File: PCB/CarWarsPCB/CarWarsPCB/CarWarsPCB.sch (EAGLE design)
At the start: 14 parts, among them J1 MAGJACK

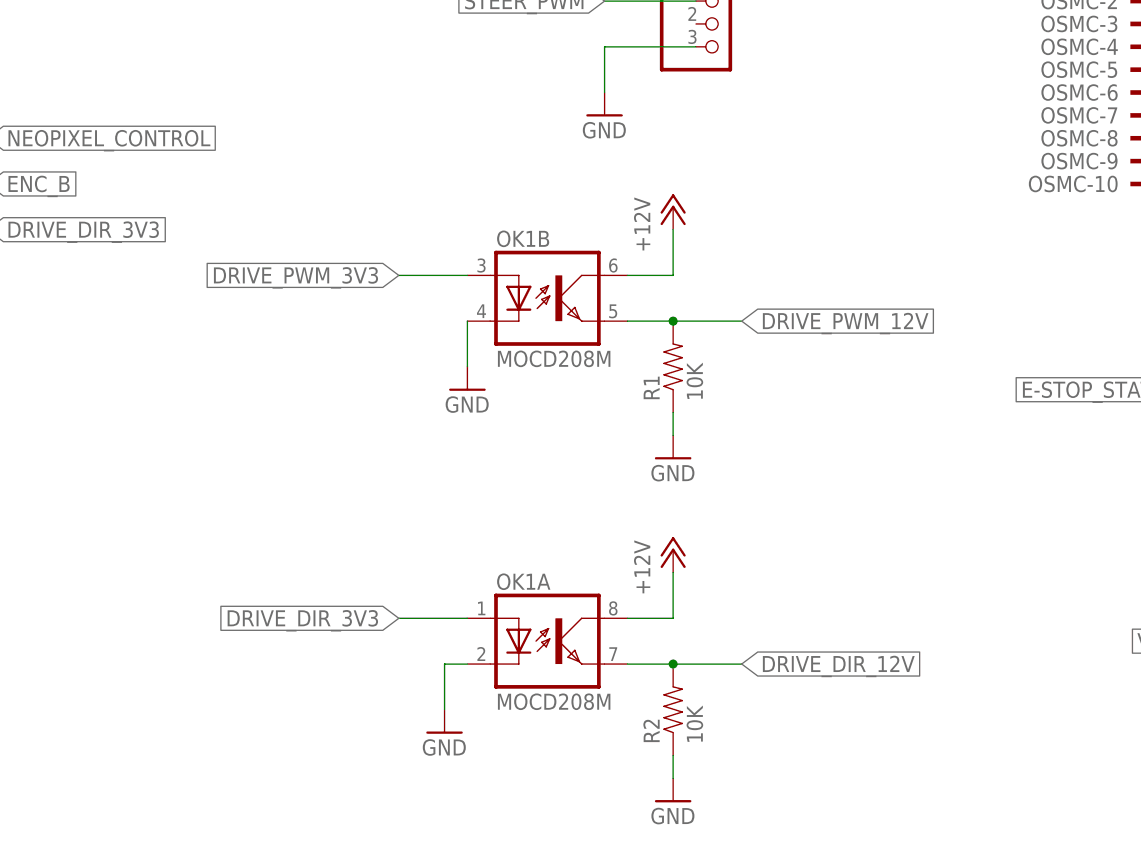
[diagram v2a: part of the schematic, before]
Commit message: CarWars PCB Prototype finalization
Implements Ryo's recommended changes to OSMC
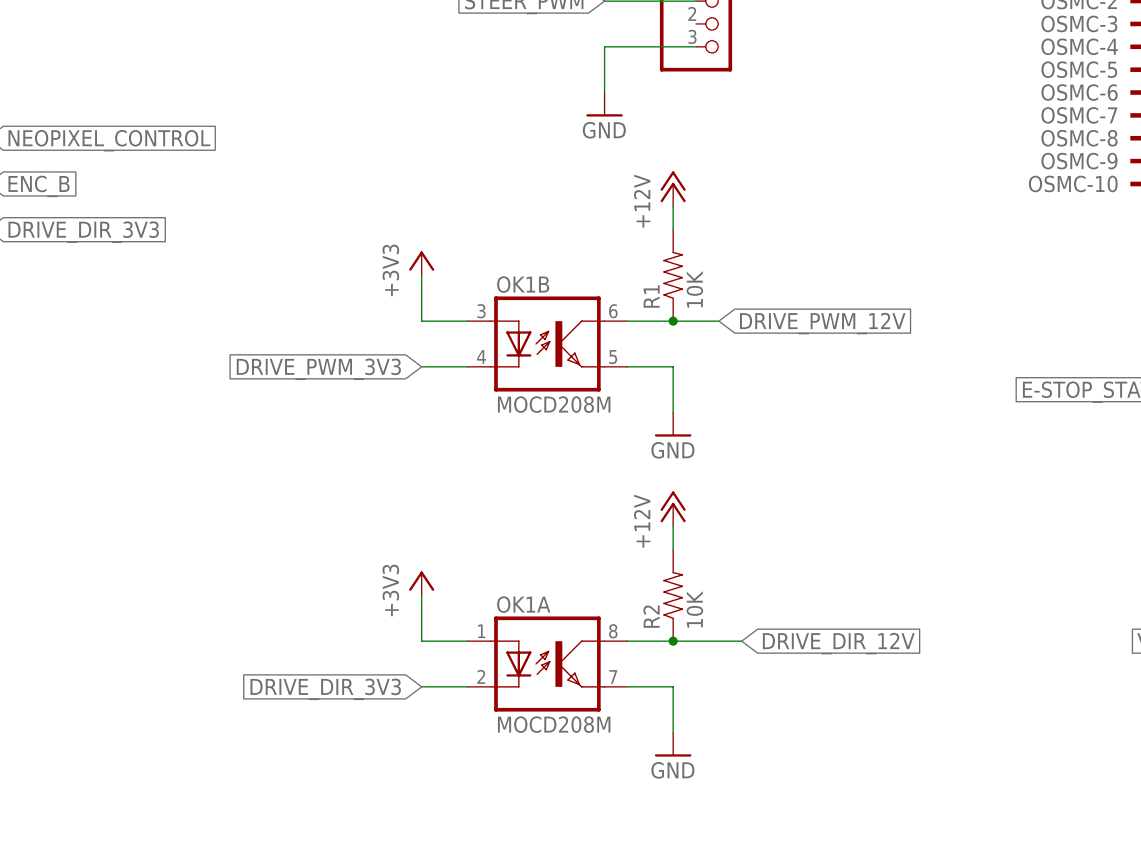
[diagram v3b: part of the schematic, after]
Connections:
- net +12V: now also R1.2, R2.2; no longer OK1A.COL, OK1B.COL
- net +3V3: now also OK1A.A, OK1B.A
- net DRIVE_DIR_12V: now also OK1A.COL, R2.1; no longer OK1A.EMIT, R2.2
- net DRIVE_DIR_3V3: now also OK1A.C; no longer OK1A.A
- net DRIVE_PWM_12V: now also OK1B.COL, R1.1; no longer OK1B.EMIT, R1.2
- net DRIVE_PWM_3V3: now also OK1B.C; no longer OK1B.A
- net GND: now also OK1A.EMIT, OK1B.EMIT; no longer OK1A.C, OK1B.C, R1.1, R2.1
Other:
- moved on the sheet: OK1A, OK1B, R1, R2
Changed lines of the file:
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@@
 <part name="GND6" library="supply1" library_urn="urn:adsk.eagle:library:371" deviceset="GND" device=""/>
 <part name="OSMC" library="con-3m" library_urn="urn:adsk.eagle:library:119" deviceset="2510-" device=""/>
-<part name="GND4" library="supply1" library_urn="urn:adsk.eagle:library:371" deviceset="GND" device=""/>
 <part name="GND7" library="supply1" library_urn="urn:adsk.eagle:library:371" deviceset="GND" device=""/>
 <part name="R1" library="SparkFun-Resistors" deviceset="10KOHM-1/10W-1%(0603)" device="0603" value="10K"/>
@@
 <part name="R2" library="SparkFun-Resistors" deviceset="10KOHM-1/10W-1%(0603)" device="0603" value="10K"/>
 <part name="GND8" library="supply1" library_urn="urn:adsk.eagle:library:371" deviceset="GND" device=""/>
-<part name="GND9" library="supply1" library_urn="urn:adsk.eagle:library:371" deviceset="GND" device=""/>
 <part name="GND10" library="supply1" library_urn="urn:adsk.eagle:library:371" deviceset="GND" device=""/>
 <part name="P+7" library="supply1" library_urn="urn:adsk.eagle:library:371" deviceset="+12V" device=""/>
@@
 <part name="P+9" library="supply1" library_urn="urn:adsk.eagle:library:371" deviceset="VCC" device=""/>
 <part name="IV_SENSOR" library="Roboracing" deviceset="PINHD-1X3" device=""/>
+<part name="+3V3" library="supply1" library_urn="urn:adsk.eagle:library:371" deviceset="+3V3" device=""/>
+<part name="+3V4" library="supply1" library_urn="urn:adsk.eagle:library:371" deviceset="+3V3" device=""/>
 </parts>
 <sheets>
@@
 <instance part="OSMC" gate="-9" x="266.7" y="43.18"/>
 <instance part="OSMC" gate="-10" x="266.7" y="40.64"/>
-<instance part="GND4" gate="1" x="193.04" y="17.78"/>
-<instance part="GND7" gate="1" x="215.9" y="10.16"/>
-<instance part="R1" gate="G$1" x="215.9" y="20.32" rot="R90"/>
-<instance part="OK1" gate="A" x="203.2" y="-10.16"/>
-<instance part="R2" gate="G$1" x="215.9" y="-17.78" rot="R90"/>
-<instance part="GND8" gate="1" x="215.9" y="-27.94"/>
-<instance part="GND9" gate="1" x="190.5" y="-20.32"/>
+<instance part="GND7" gate="1" x="215.9" y="12.7"/>
+<instance part="R1" gate="G$1" x="215.9" y="30.48" rot="R90"/>
+<instance part="OK1" gate="A" x="203.2" y="-12.7"/>
+<instance part="R2" gate="G$1" x="215.9" y="-5.08" rot="R90"/>
+<instance part="GND8" gate="1" x="215.9" y="-22.86"/>
 <instance part="GND10" gate="1" x="279.4" y="35.56"/>
 <instance part="P+7" gate="1" x="284.48" y="73.66"/>
-<instance part="P+4" gate="1" x="215.9" y="38.1"/>
-<instance part="P+5" gate="1" x="215.9" y="0"/>
-<instance part="OK1" gate="B" x="203.2" y="27.94"/>
+<instance part="P+4" gate="1" x="215.9" y="40.64"/>
+<instance part="P+5" gate="1" x="215.9" y="5.08"/>
+<instance part="OK1" gate="B" x="203.2" y="22.86"/>
 <instance part="LIGHTS" gate="A" x="314.96" y="106.68"/>
 <instance part="GND11" gate="1" x="304.8" y="99.06"/>
@@
 <instance part="P+9" gate="VCC" x="30.48" y="88.9"/>
 <instance part="IV_SENSOR" gate="A" x="299.72" y="-10.16"/>
+<instance part="+3V3" gate="G$1" x="187.96" y="33.02"/>
+<instance part="+3V4" gate="G$1" x="187.96" y="-2.54"/>
 </instances>
 <busses>
@@
 </segment>
 <segment>
-<wire x1="193.04" y1="25.4" x2="193.04" y2="20.32" width="0.1524" layer="91"/>
-<pinref part="GND4" gate="1" pin="GND"/>
-<pinref part="OK1" gate="B" pin="C"/>
-</segment>
-<segment>
-<pinref part="GND7" gate="1" pin="GND"/>
-<pinref part="R1" gate="G$1" pin="1"/>
-<wire x1="215.9" y1="12.7" x2="215.9" y2="15.24" width="0.1524" layer="91"/>
-</segment>
-<segment>
-<pinref part="OK1" gate="A" pin="C"/>
-<pinref part="GND9" gate="1" pin="GND"/>
-<wire x1="193.04" y1="-12.7" x2="190.5" y2="-12.7" width="0.1524" layer="91"/>
-<wire x1="190.5" y1="-12.7" x2="190.5" y2="-17.78" width="0.1524" layer="91"/>
-</segment>
-<segment>
-<pinref part="GND8" gate="1" pin="GND"/>
-<pinref part="R2" gate="G$1" pin="1"/>
-<wire x1="215.9" y1="-25.4" x2="215.9" y2="-22.86" width="0.1524" layer="91"/>
-</segment>
-<segment>
 <pinref part="OSMC" gate="-10" pin="KL"/>
 <pinref part="GND10" gate="1" pin="GND"/>
@@
 <label x="292.1" y="-12.7" size="1.778" layer="95" rot="R180" xref="yes"/>
 </segment>
+<segment>
+<pinref part="OK1" gate="B" pin="EMIT"/>
+<pinref part="GND7" gate="1" pin="GND"/>
+<wire x1="210.82" y1="20.32" x2="215.9" y2="20.32" width="0.1524" layer="91"/>
+<wire x1="215.9" y1="20.32" x2="215.9" y2="15.24" width="0.1524" layer="91"/>
+</segment>
+<segment>
+<pinref part="OK1" gate="A" pin="EMIT"/>
+<pinref part="GND8" gate="1" pin="GND"/>
+<wire x1="210.82" y1="-15.24" x2="215.9" y2="-15.24" width="0.1524" layer="91"/>
+<wire x1="215.9" y1="-15.24" x2="215.9" y2="-20.32" width="0.1524" layer="91"/>
+</segment>
 </net>
 <net name="+3V3" class="0">
@@
 <wire x1="119.38" y1="81.28" x2="119.38" y2="86.36" width="0.1524" layer="91"/>
 </segment>
+<segment>
+<pinref part="OK1" gate="B" pin="A"/>
+<pinref part="+3V3" gate="G$1" pin="+3V3"/>
+<wire x1="193.04" y1="25.4" x2="187.96" y2="25.4" width="0.1524" layer="91"/>
+<wire x1="187.96" y1="25.4" x2="187.96" y2="30.48" width="0.1524" layer="91"/>
+</segment>
+<segment>
+<pinref part="OK1" gate="A" pin="A"/>
+<pinref part="+3V4" gate="G$1" pin="+3V3"/>
+<wire x1="193.04" y1="-10.16" x2="187.96" y2="-10.16" width="0.1524" layer="91"/>
+<wire x1="187.96" y1="-10.16" x2="187.96" y2="-5.08" width="0.1524" layer="91"/>
+</segment>
 </net>
 <net name="DRIVE_PWM_3V3" class="0">
@@
 </segment>
 <segment>
-<wire x1="193.04" y1="30.48" x2="185.42" y2="30.48" width="0.1524" layer="91"/>
-<label x="185.42" y="30.48" size="1.778" layer="95" rot="R180" xref="yes"/>
-<pinref part="OK1" gate="B" pin="A"/>
+<pinref part="OK1" gate="B" pin="C"/>
+<wire x1="193.04" y1="20.32" x2="187.96" y2="20.32" width="0.1524" layer="91"/>
+<label x="187.96" y="20.32" size="1.778" layer="95" rot="R180" xref="yes"/>
 </segment>
 </net>
@@
 <net name="DRIVE_PWM_12V" class="0">
 <segment>
-<wire x1="210.82" y1="25.4" x2="215.9" y2="25.4" width="0.1524" layer="91"/>
-<pinref part="R1" gate="G$1" pin="2"/>
-<wire x1="215.9" y1="25.4" x2="223.52" y2="25.4" width="0.1524" layer="91"/>
-<junction x="215.9" y="25.4"/>
-<label x="223.52" y="25.4" size="1.778" layer="95" xref="yes"/>
-<pinref part="OK1" gate="B" pin="EMIT"/>
-</segment>
-<segment>
 <pinref part="OSMC" gate="-6" pin="KL"/>
 <wire x1="271.78" y1="50.8" x2="289.56" y2="50.8" width="0.1524" layer="91"/>
 <label x="289.56" y="50.8" size="1.778" layer="95" xref="yes"/>
 </segment>
+<segment>
+<pinref part="OK1" gate="B" pin="COL"/>
+<pinref part="R1" gate="G$1" pin="1"/>
+<wire x1="210.82" y1="25.4" x2="215.9" y2="25.4" width="0.1524" layer="91"/>
+<wire x1="215.9" y1="25.4" x2="220.98" y2="25.4" width="0.1524" layer="91"/>
+<junction x="215.9" y="25.4"/>
+<label x="220.98" y="25.4" size="1.778" layer="95" xref="yes"/>
+</segment>
 </net>
 <net name="DRIVE_DIR_12V" class="0">
-<segment>
-<pinref part="OK1" gate="A" pin="EMIT"/>
-<wire x1="210.82" y1="-12.7" x2="215.9" y2="-12.7" width="0.1524" layer="91"/>
-<pinref part="R2" gate="G$1" pin="2"/>
-<wire x1="215.9" y1="-12.7" x2="223.52" y2="-12.7" width="0.1524" layer="91"/>
-<junction x="215.9" y="-12.7"/>
-<label x="223.52" y="-12.7" size="1.778" layer="95" xref="yes"/>
-</segment>
 <segment>
 <pinref part="OSMC" gate="-8" pin="KL"/>
@@
 <label x="289.56" y="45.72" size="1.778" layer="95" xref="yes"/>
 </segment>
+<segment>
+<pinref part="OK1" gate="A" pin="COL"/>
+<pinref part="R2" gate="G$1" pin="1"/>
+<wire x1="210.82" y1="-10.16" x2="215.9" y2="-10.16" width="0.1524" layer="91"/>
+<wire x1="215.9" y1="-10.16" x2="223.52" y2="-10.16" width="0.1524" layer="91"/>
+<junction x="215.9" y="-10.16"/>
+<label x="223.52" y="-10.16" size="1.778" layer="95" xref="yes"/>
+</segment>
 </net>
 <net name="DRIVE_DIR_3V3" class="0">
-<segment>
-<pinref part="OK1" gate="A" pin="A"/>
-<wire x1="193.04" y1="-7.62" x2="185.42" y2="-7.62" width="0.1524" layer="91"/>
-<label x="185.42" y="-7.62" size="1.778" layer="95" rot="R180" xref="yes"/>
-</segment>
 <segment>
 <pinref part="MBED" gate="G$1" pin="P$22"/>
 <wire x1="114.3" y1="35.56" x2="139.7" y2="35.56" width="0.1524" layer="91"/>
 <label x="139.7" y="35.56" size="1.778" layer="95" xref="yes"/>
+</segment>
+<segment>
+<pinref part="OK1" gate="A" pin="C"/>
+<wire x1="193.04" y1="-15.24" x2="187.96" y2="-15.24" width="0.1524" layer="91"/>
+<label x="187.96" y="-15.24" size="1.778" layer="95" rot="R180" xref="yes"/>
 </segment>
 </net>
@@
 </segment>
 <segment>
-<wire x1="210.82" y1="30.48" x2="215.9" y2="30.48" width="0.1524" layer="91"/>
-<wire x1="215.9" y1="30.48" x2="215.9" y2="35.56" width="0.1524" layer="91"/>
 <pinref part="P+4" gate="1" pin="+12V"/>
-<pinref part="OK1" gate="B" pin="COL"/>
-</segment>
-<segment>
-<pinref part="OK1" gate="A" pin="COL"/>
-<wire x1="210.82" y1="-7.62" x2="215.9" y2="-7.62" width="0.1524" layer="91"/>
-<wire x1="215.9" y1="-7.62" x2="215.9" y2="-2.54" width="0.1524" layer="91"/>
+<pinref part="R1" gate="G$1" pin="2"/>
+<wire x1="215.9" y1="38.1" x2="215.9" y2="35.56" width="0.1524" layer="91"/>
+</segment>
+<segment>
 <pinref part="P+5" gate="1" pin="+12V"/>
-</segment>
-</net>
+<pinref part="R2" gate="G$1" pin="2"/>
+<wire x1="215.9" y1="0" x2="215.9" y2="2.54" width="0.1524" layer="91"/>
+</segment>
+</net>

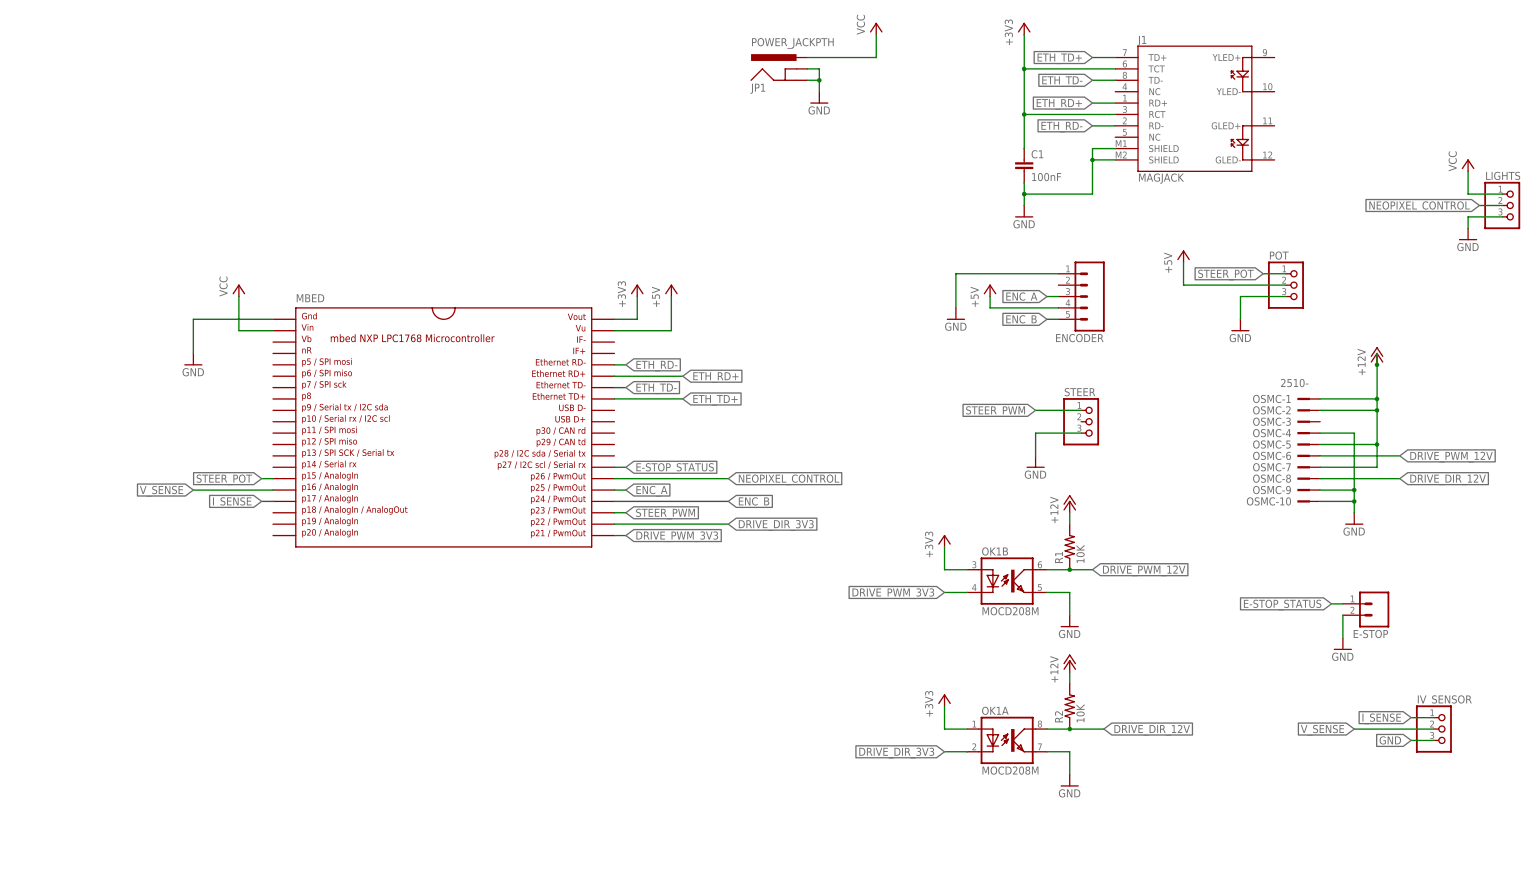
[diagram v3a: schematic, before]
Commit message: Added ground changes, 3.3V to 5V logic shifter, diode to prevent mbed powering neopixel
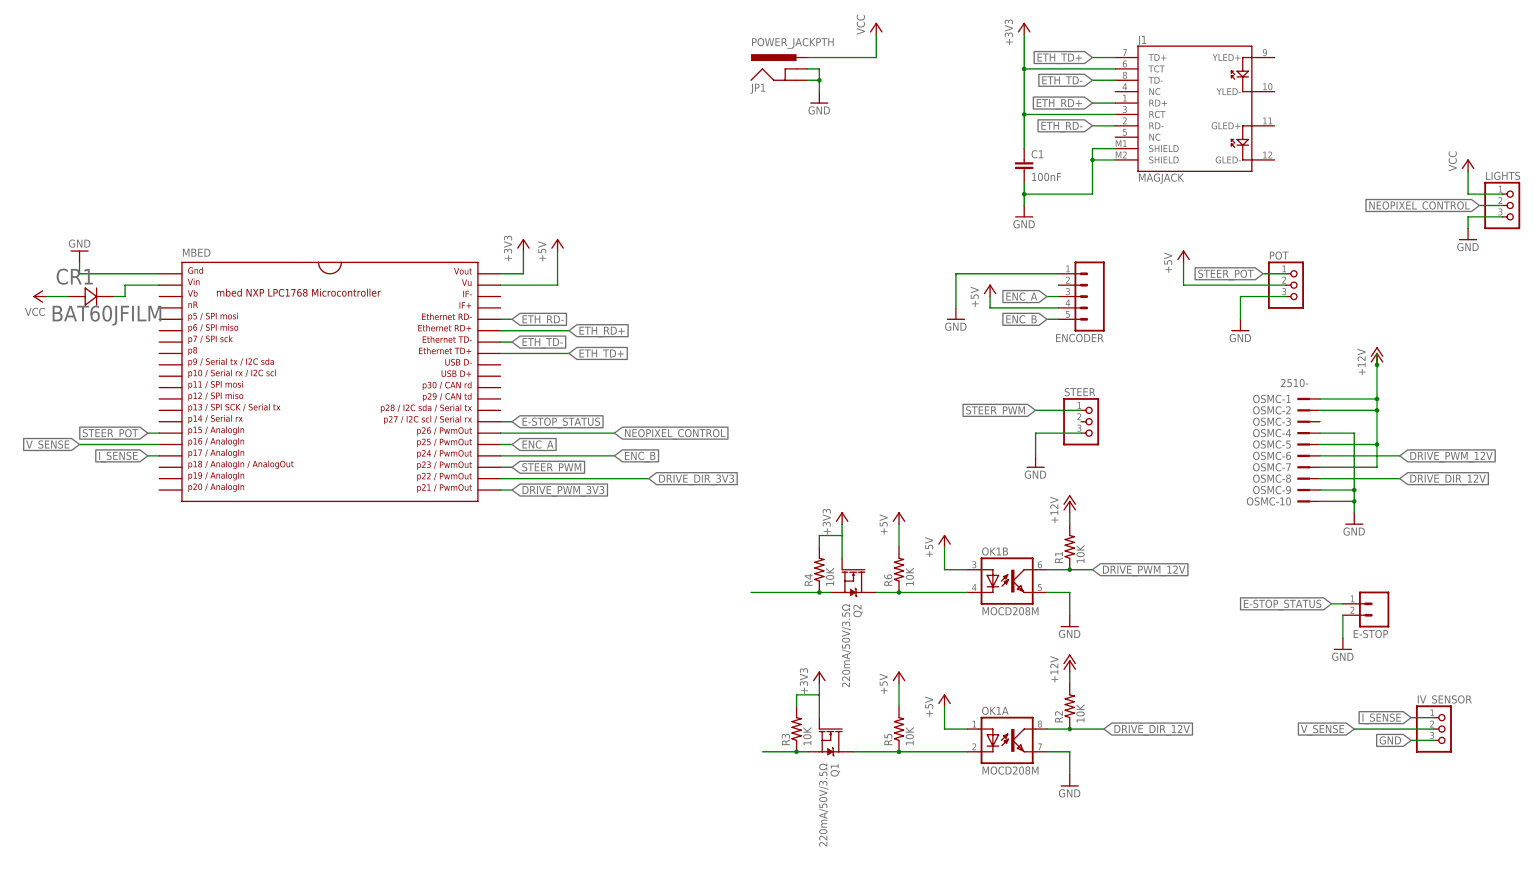
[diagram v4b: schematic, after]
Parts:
- added CR1: BAT60JFILM, Digikey:BAT60JFILM
- added Q1, Q2: 220mA/50V/3.5Ω, SparkFun-DiscreteSemi:MOSFET-NCH-BSS138
- added R3, R4, R5, R6: 10K, rcl:R-US_R0603
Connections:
- new net DGND: OK1A.EMIT, OK1B.EMIT, OSMC-10.KL, OSMC-4.KL, OSMC-9.KL
- new net N$1: CR1.11, MBED.P$2
- new net N$2: OK1A.C, Q1.D, R5.1
- new net N$3: OK1B.C, Q2.D, R6.1
- net +3V3: now also Q1.G, Q2.G, R3.2, R4.2; no longer OK1A.A, OK1B.A
- net +5V: now also OK1A.A, OK1B.A, R5.2, R6.2
- net DRIVE_DIR_3V3: now also Q1.S, R3.1; no longer OK1A.C
- net DRIVE_PWM_3V3: now also Q2.S, R4.1; no longer OK1B.C
- net GND: no longer OK1A.EMIT, OK1B.EMIT, OSMC-10.KL, OSMC-4.KL, OSMC-9.KL
- net VCC: now also CR1.22; no longer MBED.P$2
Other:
- moved on the sheet: MBED
